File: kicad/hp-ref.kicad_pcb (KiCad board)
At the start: 2 copper layers, 52.1 x 43.2 mm, 24 parts, among them J400 22-17-2052, J401 22-17-2052, Q401 MJE182, U401 LTZ1000A, U402 LT1013, X411 15k, X411412 1k / 15k, X412 1k, X414 111

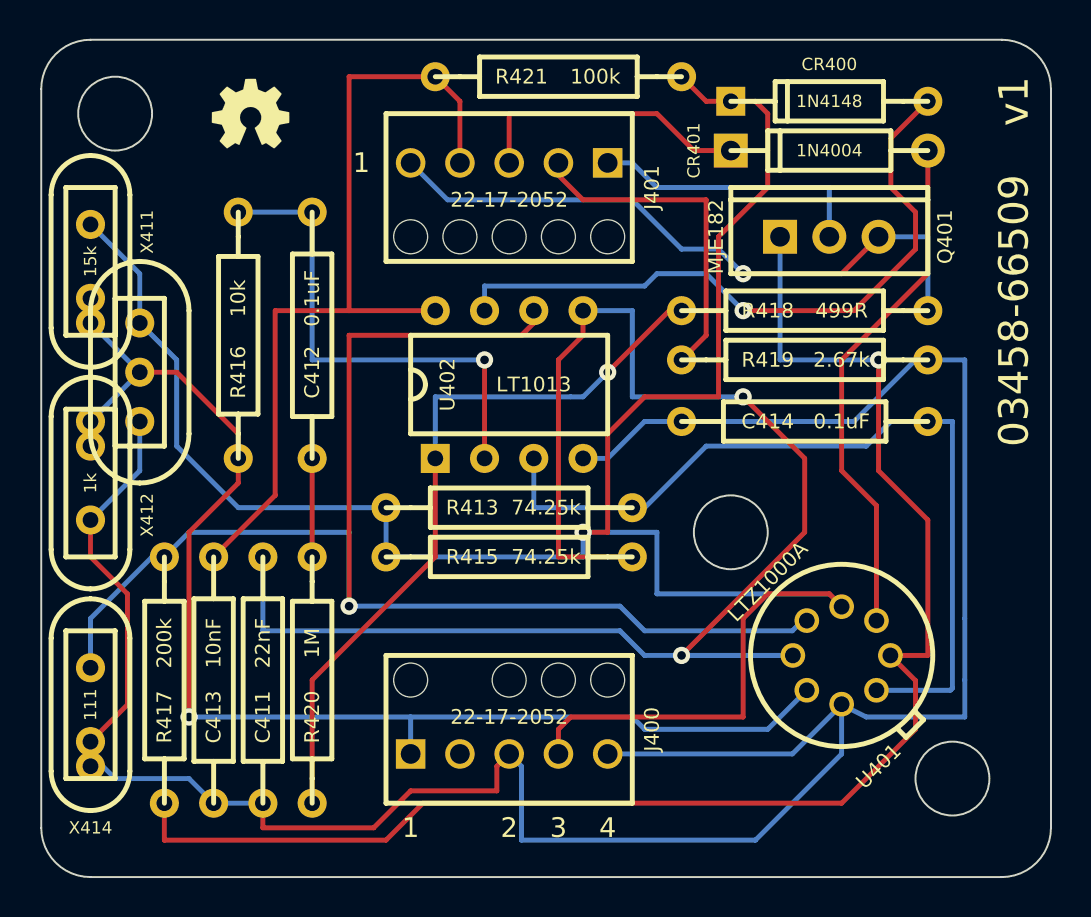
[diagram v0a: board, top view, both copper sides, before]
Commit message: board now fits within 50x50mm.  using drill rather than cutouts for mounting holes.
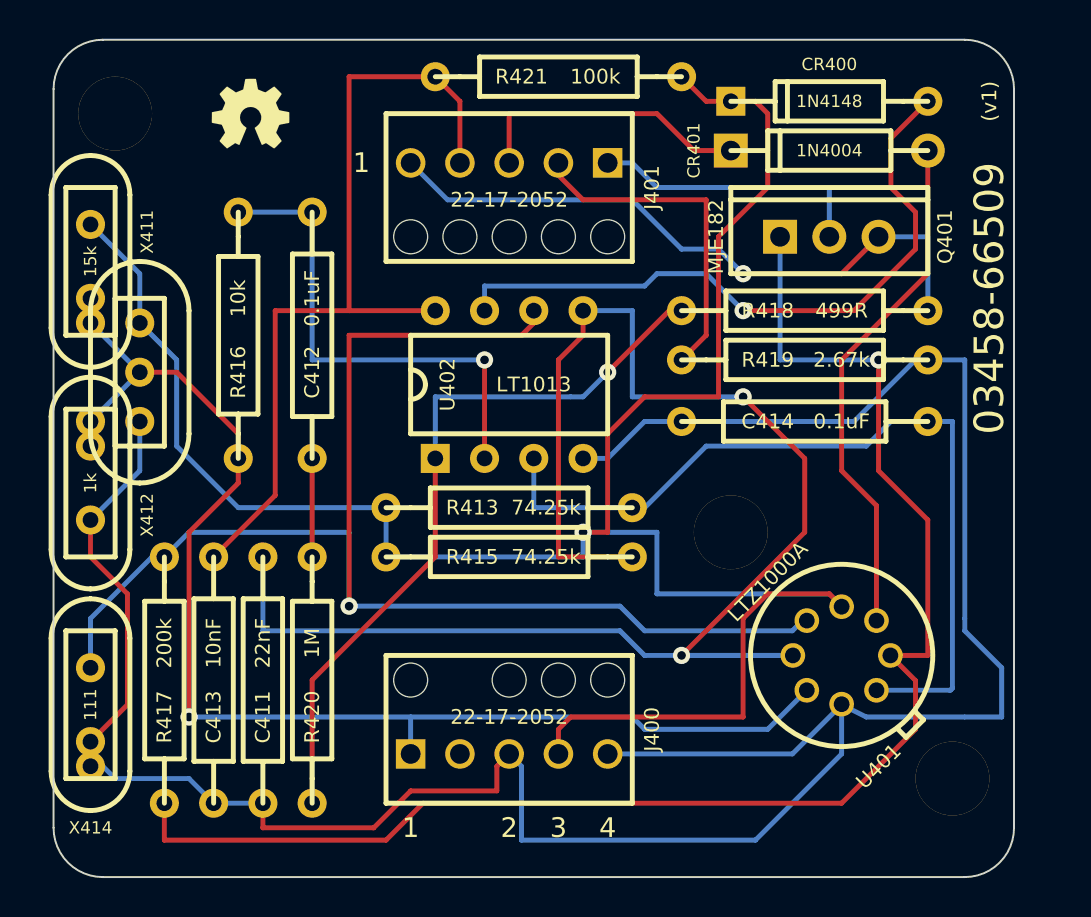
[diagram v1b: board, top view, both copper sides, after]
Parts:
- added H***: Val**, hole_15, F.Cu at (186.7, 122.6)
- added H***: Val**, hole_15, F.Cu at (218.4, 144.1)
- added H***: Val**, hole_15, F.Cu at (229.9, 156.8)
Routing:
- net J400 (2): track 131.9 -> 134.6 mm
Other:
- board size 52.1 x 43.2 mm -> 49.5 x 43.2 mm
- board text added: "(v1)"
- board text removed: "v1"
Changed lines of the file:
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@@
     (links 51)
     (no_connects 0)
-    (area 182.829999 118.694999 251.918409 161.975001)
+    (area 183.006999 118.694999 248.289233 161.975001)
     (thickness 1.6)
-    (drawings 19)
-    (tracks 215)
+    (drawings 16)
+    (tracks 217)
     (zones 0)
-    (modules 24)
+    (modules 27)
     (nets 18)
   )
@@
     (mod_text_size 1 1)
     (mod_text_width 0.15)
-    (pad_size 1.5 1.5)
-    (pad_drill 0.6)
+    (pad_size 3.81 3.81)
+    (pad_drill 3.81)
     (pad_to_mask_clearance 0)
     (aux_axis_origin 0 0)
@@
       (xy -1.21158 1.79578)) (layer F.SilkS) (width 0.00254))
   )
-  (gr_text v1 (at 233.045 121.92 90) (layer F.SilkS)
-    (effects (font (size 1.524 1.524) (thickness 0.3048)))
-  )
-  (gr_text github.com/pepaslabs/hp-03458-66509-clone (at 233.045 139.7 90) (layer B.SilkS)
-    (effects (font (size 1.016 1.016) (thickness 0.2032)) (justify mirror))
-  )
-  (gr_text 03458-66509 (at 233.045 132.715 90) (layer F.SilkS)
+  (module hole_15 (layer F.Cu)
+    (at 186.69 122.555)
+    (descr "0.15\" mounting hole")
+    (path 1pin)
+    (fp_text reference H*** (at 0 -3.048) (layer F.SilkS) hide
+      (effects (font (size 1.016 1.016) (thickness 0.254)))
+    )
+    (fp_text value Val** (at 0 2.794) (layer F.SilkS) hide
+      (effects (font (size 1.016 1.016) (thickness 0.254)))
+    )
+    (pad 1 thru_hole circle (at 0 0) (size 3.81 3.81) (drill 3.81)
+      (layers *.Cu *.Mask F.SilkS)
+    )
+  )
+  (module hole_15 (layer F.Cu)
+    (at 218.44 144.145)
+    (descr "0.15\" mounting hole")
+    (path 1pin)
+    (fp_text reference H*** (at 0 -3.048) (layer F.SilkS) hide
+      (effects (font (size 1.016 1.016) (thickness 0.254)))
+    )
+    (fp_text value Val** (at 0 2.794) (layer F.SilkS) hide
+      (effects (font (size 1.016 1.016) (thickness 0.254)))
+    )
+    (pad 1 thru_hole circle (at 0 0) (size 3.81 3.81) (drill 3.81)
+      (layers *.Cu *.Mask F.SilkS)
+    )
+  )
+  (module hole_15 (layer F.Cu)
+    (at 229.87 156.845)
+    (descr "0.15\" mounting hole")
+    (path 1pin)
+    (fp_text reference H*** (at 0 -3.048) (layer F.SilkS) hide
+      (effects (font (size 1.016 1.016) (thickness 0.254)))
+    )
+    (fp_text value Val** (at 0 2.794) (layer F.SilkS) hide
+      (effects (font (size 1.016 1.016) (thickness 0.254)))
+    )
+    (pad 1 thru_hole circle (at 0 0) (size 3.81 3.81) (drill 3.81)
+      (layers *.Cu *.Mask F.SilkS)
+    )
+  )
+  (gr_line (start 230.505 161.925) (end 186.055 161.925) (angle 90) (layer Edge.Cuts) (width 0.1))
+  (gr_line (start 186.055 118.745) (end 230.505 118.745) (angle 90) (layer Edge.Cuts) (width 0.1))
+  (gr_text "(v1)" (at 231.775 121.92 90) (layer F.SilkS)
+    (effects (font (size 0.762 0.762) (thickness 0.1524)))
+  )
+  (gr_text github.com/pepaslabs/hp-03458-66509-clone (at 231.775 137.795 90) (layer B.SilkS)
+    (effects (font (size 0.889 0.889) (thickness 0.1778)) (justify mirror))
+  )
+  (gr_text 03458-66509 (at 231.775 132.08 90) (layer F.SilkS)
     (effects (font (size 1.524 1.524) (thickness 0.3048)))
   )
@@
     (effects (font (size 1.016 1.016) (thickness 0.2032)))
   )
-  (gr_circle (center 218.44 144.145) (end 220.345 144.145) (layer Edge.Cuts) (width 0.1))
-  (gr_circle (center 229.87 156.845) (end 231.775 156.845) (layer Edge.Cuts) (width 0.1))
-  (gr_circle (center 186.69 122.555) (end 188.595 122.555) (layer Edge.Cuts) (width 0.1))
-  (gr_line (start 234.95 121.285) (end 234.95 159.385) (angle 90) (layer Edge.Cuts) (width 0.1))
-  (gr_line (start 182.88 159.385) (end 182.88 121.285) (angle 90) (layer Edge.Cuts) (width 0.1))
-  (gr_line (start 232.41 161.925) (end 185.42 161.925) (angle 90) (layer Edge.Cuts) (width 0.1))
-  (gr_line (start 185.42 118.745) (end 232.41 118.745) (angle 90) (layer Edge.Cuts) (width 0.1))
-  (gr_arc (start 185.42 159.385) (end 185.42 161.925) (angle 90) (layer Edge.Cuts) (width 0.1))
-  (gr_arc (start 232.41 159.385) (end 234.95 159.385) (angle 90) (layer Edge.Cuts) (width 0.1))
-  (gr_arc (start 232.41 121.285) (end 232.41 118.745) (angle 90) (layer Edge.Cuts) (width 0.1))
-  (gr_arc (start 185.42 121.285) (end 182.88 121.285) (angle 90) (layer Edge.Cuts) (width 0.1))
+  (gr_line (start 233.045 121.285) (end 233.045 159.385) (angle 90) (layer Edge.Cuts) (width 0.1))
+  (gr_line (start 183.515 159.385) (end 183.515 121.285) (angle 90) (layer Edge.Cuts) (width 0.1))
+  (gr_arc (start 186.055 159.385) (end 186.055 161.925) (angle 90) (layer Edge.Cuts) (width 0.1))
+  (gr_arc (start 230.505 159.385) (end 233.045 159.385) (angle 90) (layer Edge.Cuts) (width 0.1))
+  (gr_arc (start 230.505 121.285) (end 230.505 118.745) (angle 90) (layer Edge.Cuts) (width 0.1))
+  (gr_arc (start 186.055 121.285) (end 183.515 121.285) (angle 90) (layer Edge.Cuts) (width 0.1))
   (segment (start 204.47 125.095) (end 204.47 121.92) (width 0.254) (layer F.Cu) (net 1))
   (segment (start 204.47 121.92) (end 203.2 120.65) (width 0.254) (layer F.Cu) (net 1))
@@
   (segment (start 213.995 154.305) (end 213.36 153.67) (width 0.254) (layer B.Cu) (net 6))
   (segment (start 220.345 154.305) (end 213.995 154.305) (width 0.254) (layer B.Cu) (net 6))
+  (segment (start 230.505 153.67) (end 232.41 153.67) (width 0.254) (layer B.Cu) (net 7))
+  (segment (start 232.41 151.13) (end 230.505 149.225) (width 0.254) (layer B.Cu) (net 7))
+  (segment (start 232.41 153.67) (end 232.41 151.13) (width 0.254) (layer B.Cu) (net 7))
   (segment (start 224.155 153.035) (end 224.155 153.009472) (width 0.254) (layer B.Cu) (net 7))
   (segment (start 185.42 143.51) (end 185.42 145.415) (width 0.254) (layer F.Cu) (net 7))
@@
   (segment (start 207.645 156.21) (end 207.01 155.575) (width 0.254) (layer B.Cu) (net 7))
   (segment (start 230.505 148.59) (end 230.505 148.59) (width 0.254) (layer B.Cu) (net 7))
-  (segment (start 230.505 151.765) (end 230.505 153.67) (width 0.254) (layer B.Cu) (net 7))
   (segment (start 224.155 153.035) (end 225.425 153.67) (width 0.254) (layer B.Cu) (net 7))
   (segment (start 225.425 153.67) (end 230.505 153.67) (width 0.254) (layer B.Cu) (net 7))
-  (segment (start 230.505 148.59) (end 230.505 151.765) (width 0.254) (layer B.Cu) (net 7))
+  (segment (start 230.505 148.59) (end 230.505 149.225) (width 0.254) (layer B.Cu) (net 7))
   (segment (start 230.505 135.255) (end 228.6 135.255) (width 0.254) (layer B.Cu) (net 7))
   (segment (start 230.505 148.59) (end 230.505 135.255) (width 0.254) (layer B.Cu) (net 7))

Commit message: v2: better alignment and hermetic options for R413 and R415.
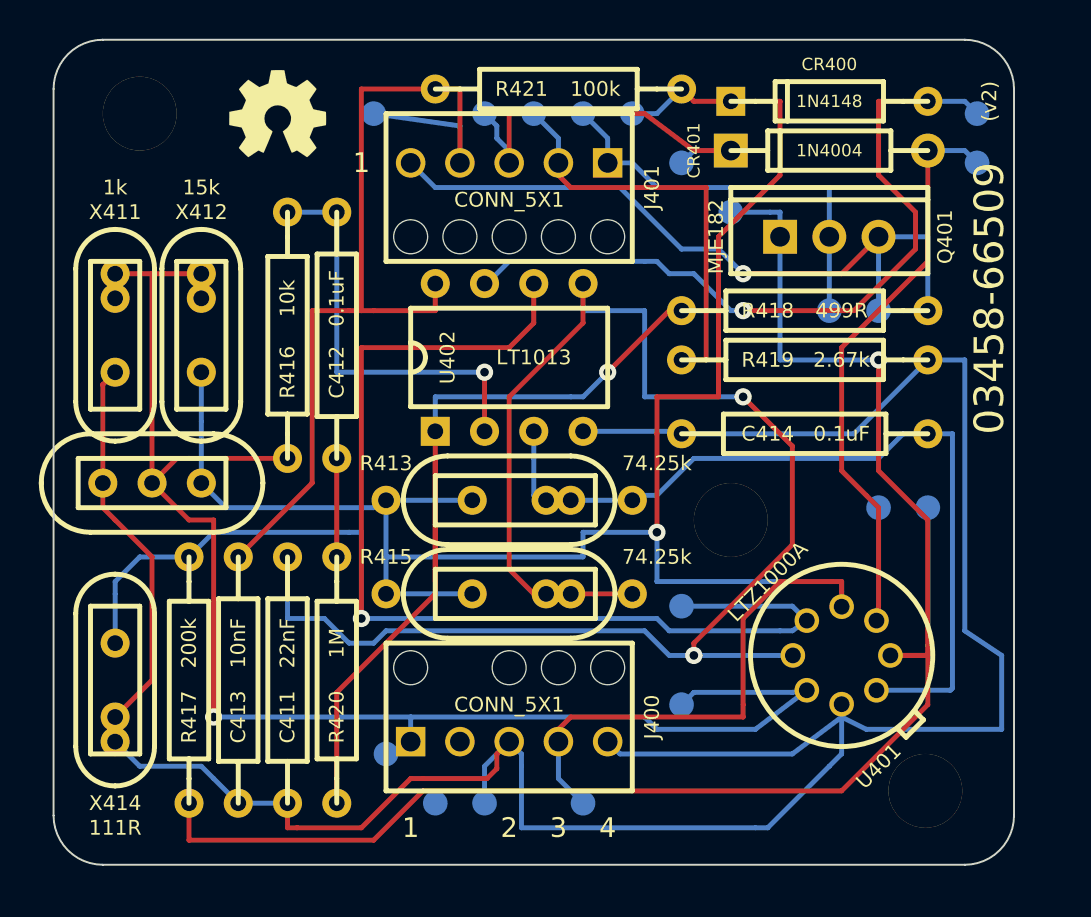
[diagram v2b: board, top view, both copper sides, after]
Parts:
- removed the G*** at (193.7, 122.6)
- added G***: OSHW-logo_silkscreen-front_5mm, OSHW-logo_silkscreen-front_5mm, F.Cu at (195.1, 122.6)
- added TEST_SMD_05: VAL**, TEST_SMD_02, B.Cu at (231.1, 122.6)
- added TEST_SMD_05: VAL**, TEST_SMD_02, F.Cu at (223.5, 132.7)
- added TEST_SMD_05: VAL**, TEST_SMD_02, B.Cu at (218.4, 127.6)
- added TEST_SMD_05: VAL**, TEST_SMD_02, F.Cu at (200.7, 155.6)
- added TEST_SMD_05: VAL**, TEST_SMD_02, F.Cu at (203.2, 158.1)
- added TEST_SMD_05: VAL**, TEST_SMD_02, F.Cu at (205.7, 158.1)
- added TEST_SMD_05: VAL**, TEST_SMD_02, F.Cu at (210.8, 158.1)
- added TEST_SMD_05: VAL**, TEST_SMD_02, F.Cu at (228.6, 142.9)
- added TEST_SMD_05: VAL**, TEST_SMD_02, F.Cu at (226.1, 142.9)
- added TEST_SMD_05: VAL**, TEST_SMD_02, B.Cu at (215.9, 153.0)
- added TEST_SMD_05: VAL**, TEST_SMD_02, B.Cu at (215.9, 148.0)
- added TEST_SMD_05: VAL**, TEST_SMD_02, B.Cu at (231.1, 125.1)
- added TEST_SMD_05: VAL**, TEST_SMD_02, B.Cu at (215.9, 125.1)
- added TEST_SMD_05: VAL**, TEST_SMD_02, B.Cu at (213.4, 122.6)
- added TEST_SMD_05: VAL**, TEST_SMD_02, F.Cu at (210.8, 122.6)
- added TEST_SMD_05: VAL**, TEST_SMD_02, F.Cu at (208.3, 122.6)
- added TEST_SMD_05: VAL**, TEST_SMD_02, F.Cu at (205.7, 122.6)
- added TEST_SMD_05: VAL**, TEST_SMD_02, F.Cu at (200.0, 122.6)
- added TEST_SMD_05: VAL**, TEST_SMD_02, F.Cu at (226.1, 132.7)
- J400, J401: value 22-17-2052 -> CONN_5X1
- R413, R415: footprint R_AXIAL_0W25_059A_05_PL -> R_BOX_HERMETIC_AXIAL_05_PL
- X411412: value 1k / 15k -> 15k / 1k
- X414: value 111 -> 111R
- moved X412 7.73 mm to (186.7, 132.1)
- moved R415 6.63 mm to (207.0, 147.3)
- moved R413 6.36 mm to (207.0, 142.5)
- moved X411412 5.75 mm to (188.6, 141.6), turned to 180 degrees
- moved X411 5.72 mm to (191.1, 132.1), turned to 270 degrees
- moved R416 2.54 mm to (195.6, 140.3)
- moved X414 1.80 mm to (186.7, 153.7)
- moved H*** 1.53 mm to (228.5, 157.5)
- moved U402 1.40 mm to (203.2, 138.9)
- moved C411 1.27 mm to (195.6, 151.8)
- moved C412 1.27 mm to (198.1, 134.0)
- moved H*** 1.27 mm to (188.0, 122.6)
- moved R417 1.27 mm to (190.5, 158.1)
- moved R420 1.27 mm to (198.1, 145.4)
- moved C413 1.27 mm to (193.0, 151.8)
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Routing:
- net J400 (1): track 66.6 -> 80.4 mm
- net N-000001: track 77.0 -> 90.5 mm
- net N-000002: track 26.8 -> 35.5 mm
- net +7: track 111.9 -> 119.8 mm
- net +18H: track 14.5 -> 21.4 mm
- net N-000007: track 70.3 -> 77.0 mm
- net (no net): track 0.00 -> 6.35 mm
- net H GND: track 14.8 -> 20.5 mm
- net +18: track 43.8 -> 48.7 mm
- net J400 (2): track 134.6 -> 139.0 mm
- net -15: track 17.6 -> 21.7 mm
- net N-000009: track 34.8 -> 38.8 mm
- net N-0000011: track 25.4 -> 21.5 mm
- net J401 (1): track 33.6 -> 37.4 mm
- net N-0000010: track 38.1 -> 37.6 mm
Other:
- board size 49.5 x 43.2 mm -> 49.5 x 42.5 mm
- board text added: "(v2)"
- board text removed: "(v1)"
